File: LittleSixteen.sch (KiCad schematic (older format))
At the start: 0 parts

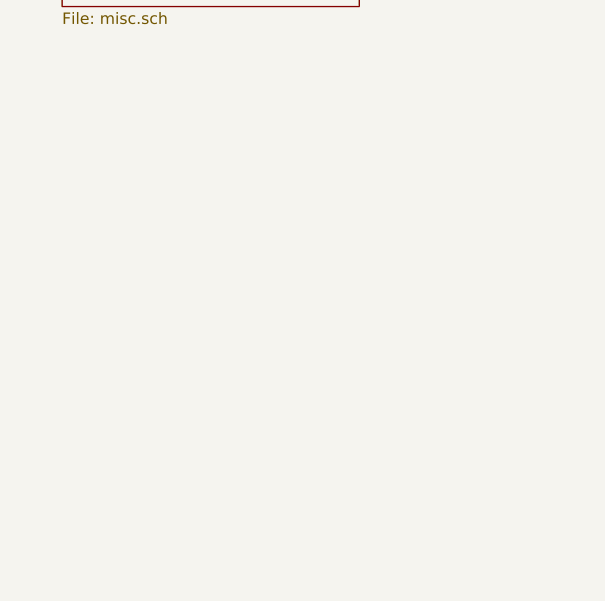
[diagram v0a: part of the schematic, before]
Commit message: Add holes and exposed copper areas
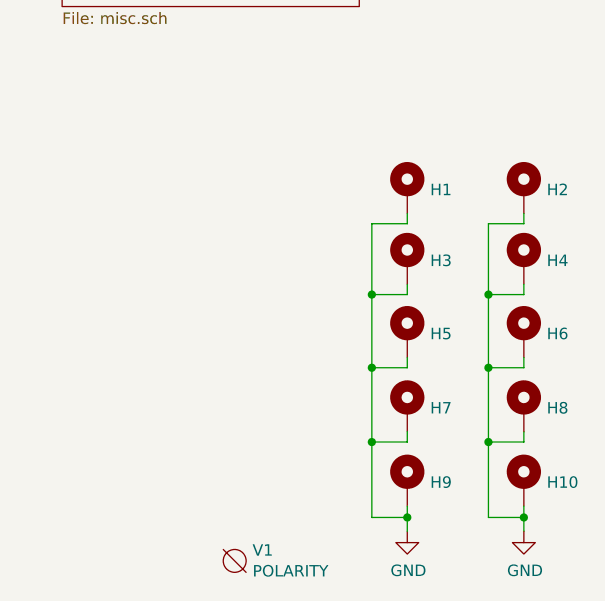
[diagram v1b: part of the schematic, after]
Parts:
- added H1, H2, H3, H4, H5, H6, H7: MountingHole_Pad, MountingHole:MountingHole_3.7mm_Pad, symbol Mechanical:MountingHole_Pad
- added H10, H8, H9: MountingHole_Pad, MountingHole:MountingHole_4.3mm_M4_Pad, symbol Mechanical:MountingHole_Pad
- added V1: POLARITY, w_logo:Logo_silk_polarity_external_10x2.8mm, symbol void:Void
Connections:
- new net GND: H1.1, H10.1, H2.1, H3.1, H4.1, H5.1, H6.1, H7.1, H8.1, H9.1
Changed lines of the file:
@@
 Sheet 1 11
 Title "LittleSixteen"
-Date "2020-01-03"
+Date "2021-07-16"
 Rev "1git"
 Comp "SukkoPera"
@@
 F1 "avout.sch" 50
 $EndSheet
+$Comp
+L Mechanical:MountingHole_Pad H1
+U 1 1 61150450
+P 10320 4735
+F 0 "H1" H 10420 4738 50  0000 L CNN
+F 1 "MountingHole_Pad" H 10420 4693 50  0001 L CNN
+F 2 "MountingHole:MountingHole_3.7mm_Pad" H 10320 4735 50  0001 C CNN
+F 3 "~" H 10320 4735 50  0001 C CNN
+	1    10320 4735
+	1    0    0    -1
+$EndComp
+$Comp
+L Mechanical:MountingHole_Pad H3
+U 1 1 61150D7C
+P 10320 5045
+F 0 "H3" H 10420 5048 50  0000 L CNN
+F 1 "MountingHole_Pad" H 10420 5003 50  0001 L CNN
+F 2 "MountingHole:MountingHole_3.7mm_Pad" H 10320 5045 50  0001 C CNN
+F 3 "~" H 10320 5045 50  0001 C CNN
+	1    10320 5045
+	1    0    0    -1
+$EndComp
+$Comp
+L Mechanical:MountingHole_Pad H5
+U 1 1 611511B9
+P 10320 5365
+F 0 "H5" H 10420 5368 50  0000 L CNN
+F 1 "MountingHole_Pad" H 10420 5323 50  0001 L CNN
+F 2 "MountingHole:MountingHole_3.7mm_Pad" H 10320 5365 50  0001 C CNN
+F 3 "~" H 10320 5365 50  0001 C CNN
+	1    10320 5365
+	1    0    0    -1
+$EndComp
+$Comp
+L Mechanical:MountingHole_Pad H7
+U 1 1 611515CC
+P 10320 5690
+F 0 "H7" H 10420 5693 50  0000 L CNN
+F 1 "MountingHole_Pad" H 10420 5648 50  0001 L CNN
+F 2 "MountingHole:MountingHole_3.7mm_Pad" H 10320 5690 50  0001 C CNN
+F 3 "~" H 10320 5690 50  0001 C CNN
+	1    10320 5690
+	1    0    0    -1
+$EndComp
+$Comp
+L Mechanical:MountingHole_Pad H9
+U 1 1 61151934
+P 10320 6015
+F 0 "H9" H 10420 6018 50  0000 L CNN
+F 1 "MountingHole_Pad" H 10420 5973 50  0001 L CNN
+F 2 "MountingHole:MountingHole_4.3mm_M4_Pad" H 10320 6015 50  0001 C CNN
+F 3 "~" H 10320 6015 50  0001 C CNN
+	1    10320 6015
+	1    0    0    -1
+$EndComp
+Wire Wire Line
+	10165 6165 10320 6165
+Wire Wire Line
+	10320 6165 10320 6225
+$Comp
+L power:GND #PWR0185
+U 1 1 61151F98
+P 10320 6225
+F 0 "#PWR0185" H 10320 5975 50  0001 C CNN
+F 1 "GND" H 10325 6052 50  0000 C CNN
+F 2 "" H 10320 6225 50  0001 C CNN
+F 3 "" H 10320 6225 50  0001 C CNN
+	1    10320 6225
+	1    0    0    -1
+$EndComp
+Wire Wire Line
+	10320 6165 10320 6115
+Connection ~ 10320 6165
+Wire Wire Line
+	10320 5790 10320 5835
+Wire Wire Line
+	10320 5835 10165 5835
+Connection ~ 10165 5835
+Wire Wire Line
+	10165 5835 10165 6165
+Wire Wire Line
+	10320 5465 10320 5510
+Wire Wire Line
+	10320 5510 10165 5510
+Connection ~ 10165 5510
+Wire Wire Line
+	10165 5510 10165 5835
+Wire Wire Line
+	10320 5145 10320 5190
+Wire Wire Line
+	10320 5190 10165 5190
+Connection ~ 10165 5190
+Wire Wire Line
+	10165 5190 10165 5510
+Wire Wire Line
+	10320 4835 10320 4880
+Wire Wire Line
+	10320 4880 10165 4880
+Wire Wire Line
+	10165 4880 10165 5190
+$Comp
+L Mechanical:MountingHole_Pad H2
+U 1 1 61152AD4
+P 10830 4735
+F 0 "H2" H 10930 4738 50  0000 L CNN
+F 1 "MountingHole_Pad" H 10930 4693 50  0001 L CNN
+F 2 "MountingHole:MountingHole_3.7mm_Pad" H 10830 4735 50  0001 C CNN
+F 3 "~" H 10830 4735 50  0001 C CNN
+	1    10830 4735
+	1    0    0    -1
+$EndComp
+$Comp
+L Mechanical:MountingHole_Pad H4
+U 1 1 61152B3A
+P 10830 5045
+F 0 "H4" H 10930 5048 50  0000 L CNN
+F 1 "MountingHole_Pad" H 10930 5003 50  0001 L CNN
+F 2 "MountingHole:MountingHole_3.7mm_Pad" H 10830 5045 50  0001 C CNN
+F 3 "~" H 10830 5045 50  0001 C CNN
+	1    10830 5045
+	1    0    0    -1
+$EndComp
+$Comp
+L Mechanical:MountingHole_Pad H6
+U 1 1 61152B44
+P 10830 5365
+F 0 "H6" H 10930 5368 50  0000 L CNN
+F 1 "MountingHole_Pad" H 10930 5323 50  0001 L CNN
+F 2 "MountingHole:MountingHole_3.7mm_Pad" H 10830 5365 50  0001 C CNN
+F 3 "~" H 10830 5365 50  0001 C CNN
+	1    10830 5365
+	1    0    0    -1
+$EndComp
+$Comp
+L Mechanical:MountingHole_Pad H8
+U 1 1 61152B4E
+P 10830 5690
+F 0 "H8" H 10930 5693 50  0000 L CNN
+F 1 "MountingHole_Pad" H 10930 5648 50  0001 L CNN
+F 2 "MountingHole:MountingHole_4.3mm_M4_Pad" H 10830 5690 50  0001 C CNN
+F 3 "~" H 10830 5690 50  0001 C CNN
+	1    10830 5690
+	1    0    0    -1
+$EndComp
+$Comp
+L Mechanical:MountingHole_Pad H10
+U 1 1 61152B58
+P 10830 6015
+F 0 "H10" H 10930 6018 50  0000 L CNN
+F 1 "MountingHole_Pad" H 10930 5973 50  0001 L CNN
+F 2 "MountingHole:MountingHole_4.3mm_M4_Pad" H 10830 6015 50  0001 C CNN
+F 3 "~" H 10830 6015 50  0001 C CNN
+	1    10830 6015
+	1    0    0    -1
+$EndComp
+Wire Wire Line
+	10675 6165 10830 6165
+Wire Wire Line
+	10830 6165 10830 6225
+$Comp
+L power:GND #PWR0186
+U 1 1 61152B64
+P 10830 6225
+F 0 "#PWR0186" H 10830 5975 50  0001 C CNN
+F 1 "GND" H 10835 6052 50  0000 C CNN
+F 2 "" H 10830 6225 50  0001 C CNN
+F 3 "" H 10830 6225 50  0001 C CNN
+	1    10830 6225
+	1    0    0    -1
+$EndComp
+Wire Wire Line
+	10830 6165 10830 6115
+Connection ~ 10830 6165
+Wire Wire Line
+	10830 5790 10830 5835
+Wire Wire Line
+	10830 5835 10675 5835
+Connection ~ 10675 5835
+Wire Wire Line
+	10675 5835 10675 6165
+Wire Wire Line
+	10830 5465 10830 5510
+Wire Wire Line
+	10830 5510 10675 5510
+Connection ~ 10675 5510
+Wire Wire Line
+	10675 5510 10675 5835
+Wire Wire Line
+	10830 5145 10830 5190
+Wire Wire Line
+	10830 5190 10675 5190
+Connection ~ 10675 5190
+Wire Wire Line
+	10675 5190 10675 5510
+Wire Wire Line
+	10830 4835 10830 4880
+Wire Wire Line
+	10830 4880 10675 4880
+Wire Wire Line
+	10675 4880 10675 5190
+$Comp
+L void:Void V1
+U 1 1 61157949
+P 9565 6355
+F 0 "V1" H 9643 6401 50  0000 L CNN
+F 1 "POLARITY" H 9643 6310 50  0000 L CNN
+F 2 "w_logo:Logo_silk_polarity_external_10x2.8mm" H 9565 6355 50  0001 C CNN
+F 3 "" H 9565 6355 50  0001 C CNN
+	1    9565 6355
+	1    0    0    -1
+$EndComp
 $EndSCHEMATC

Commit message: Work a bit on silkscreen and add logo
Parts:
- added V0: LOGO, LittleSixteen:Logo, symbol void:Void
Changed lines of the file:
@@
 Sheet 1 11
 Title "LittleSixteen"
-Date "2021-07-16"
+Date "2021-07-20"
 Rev "1git"
 Comp "SukkoPera"
@@
 	1    0    0    -1
 $EndComp
+$Comp
+L void:Void V0
+U 1 1 61145DF1
+P 9565 6150
+F 0 "V0" H 9643 6196 50  0000 L CNN
+F 1 "LOGO" H 9643 6105 50  0000 L CNN
+F 2 "LittleSixteen:Logo" H 9565 6150 50  0001 C CNN
+F 3 "" H 9565 6150 50  0001 C CNN
+	1    9565 6150
+	1    0    0    -1
+$EndComp

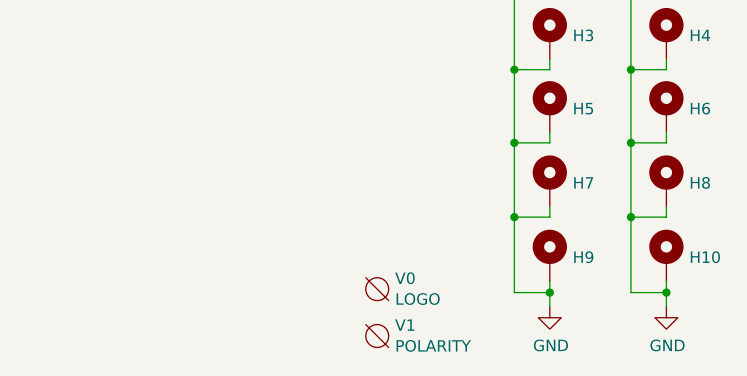
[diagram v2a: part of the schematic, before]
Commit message: Add CC logo and board URL and update README
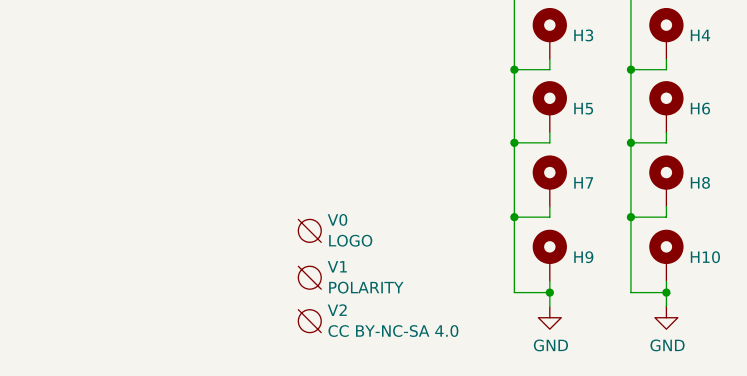
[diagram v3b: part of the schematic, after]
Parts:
- added V2: CC BY-NC-SA 4.0, LittleSixteen:cc_by_nc_sa, symbol void:Void
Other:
- moved on the sheet: V0, V1
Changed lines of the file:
@@
 L void:Void V1
 U 1 1 61157949
-P 9565 6355
-F 0 "V1" H 9643 6401 50  0000 L CNN
-F 1 "POLARITY" H 9643 6310 50  0000 L CNN
-F 2 "w_logo:Logo_silk_polarity_external_10x2.8mm" H 9565 6355 50  0001 C CNN
-F 3 "" H 9565 6355 50  0001 C CNN
-	1    9565 6355
+P 9270 6100
+F 0 "V1" H 9348 6146 50  0000 L CNN
+F 1 "POLARITY" H 9348 6055 50  0000 L CNN
+F 2 "w_logo:Logo_silk_polarity_external_10x2.8mm" H 9270 6100 50  0001 C CNN
+F 3 "" H 9270 6100 50  0001 C CNN
+	1    9270 6100
 	1    0    0    -1
 $EndComp
@@
 L void:Void V0
 U 1 1 61145DF1
-P 9565 6150
-F 0 "V0" H 9643 6196 50  0000 L CNN
-F 1 "LOGO" H 9643 6105 50  0000 L CNN
-F 2 "LittleSixteen:Logo" H 9565 6150 50  0001 C CNN
-F 3 "" H 9565 6150 50  0001 C CNN
-	1    9565 6150
+P 9270 5895
+F 0 "V0" H 9348 5941 50  0000 L CNN
+F 1 "LOGO" H 9348 5850 50  0000 L CNN
+F 2 "LittleSixteen:Logo" H 9270 5895 50  0001 C CNN
+F 3 "" H 9270 5895 50  0001 C CNN
+	1    9270 5895
 	1    0    0    -1
 $EndComp
+$Comp
+L void:Void V2
+U 1 1 61992CC0
+P 9270 6290
+F 0 "V2" H 9348 6336 50  0000 L CNN
+F 1 "CC BY-NC-SA 4.0" H 9348 6245 50  0000 L CNN
+F 2 "LittleSixteen:cc_by_nc_sa" H 9270 6290 50  0001 C CNN
+F 3 "" H 9270 6290 50  0001 C CNN
+	1    9270 6290
+	1    0    0    -1
+$EndComp
